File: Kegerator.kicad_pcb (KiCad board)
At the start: 2 copper layers, 200 x 21 mm, 17 parts, among them J1 Buttons, J2 LCD, J3 Temperature, J4 Programmer, J5 Control, U1 ESP32-S2-WROVER, U2 MCP1700

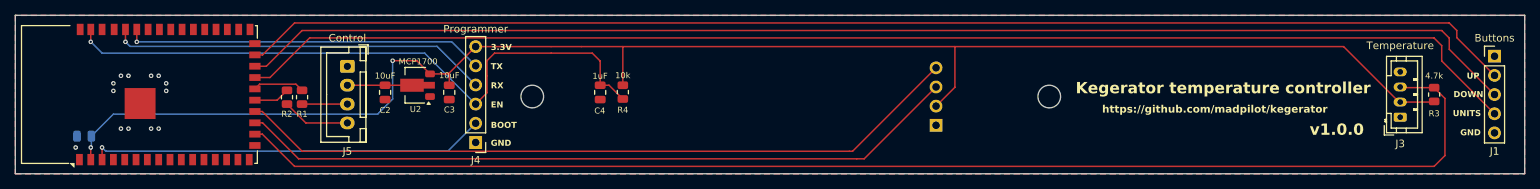
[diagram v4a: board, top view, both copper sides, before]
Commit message: STop using GPIO26
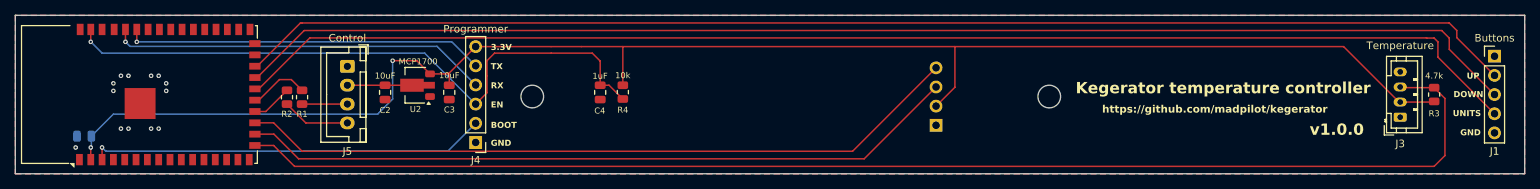
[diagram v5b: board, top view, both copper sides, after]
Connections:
- U1 pad 17: unconnected-(U1-IO14-Pad17) -> TEMP
- U1 pad 18: TEMP -> SCL
- U1 pad 19: SCL -> SDA
- U1 pad 20: SDA -> HEATER
- U1 pad 21: HEATER -> COMPRESSOR
- U1 pad 22: COMPRESSOR -> UNITS
- U1 pad 23: UNITS -> TEMP_DOWN
- U1 pad 24: TEMP_DOWN -> TEMP_UP
- U1 pad 25: TEMP_UP -> unconnected-(U1-IO26-Pad25)
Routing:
- net SCL: track 96.8 -> 95.5 mm
- net TEMP_DOWN: track 170.6 -> 171.7 mm
- net COMPRESSOR: track 6.84 -> 7.97 mm
- net TEMP: track 23.5 -> 22.5 mm
- net HEATER: track 4.79 -> 5.41 mm
- net UNITS: track 171.8 -> 172.4 mm
- net TEMP_UP: track 169.4 -> 170.1 mm
- net SDA: track 97.3 -> 96.7 mm
